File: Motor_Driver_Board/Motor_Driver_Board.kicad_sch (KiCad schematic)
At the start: 33 parts, among them J1 POWER, J2 MOTOR, J3 LCD, SW1 ENCODER, U1 XL1509-5.0

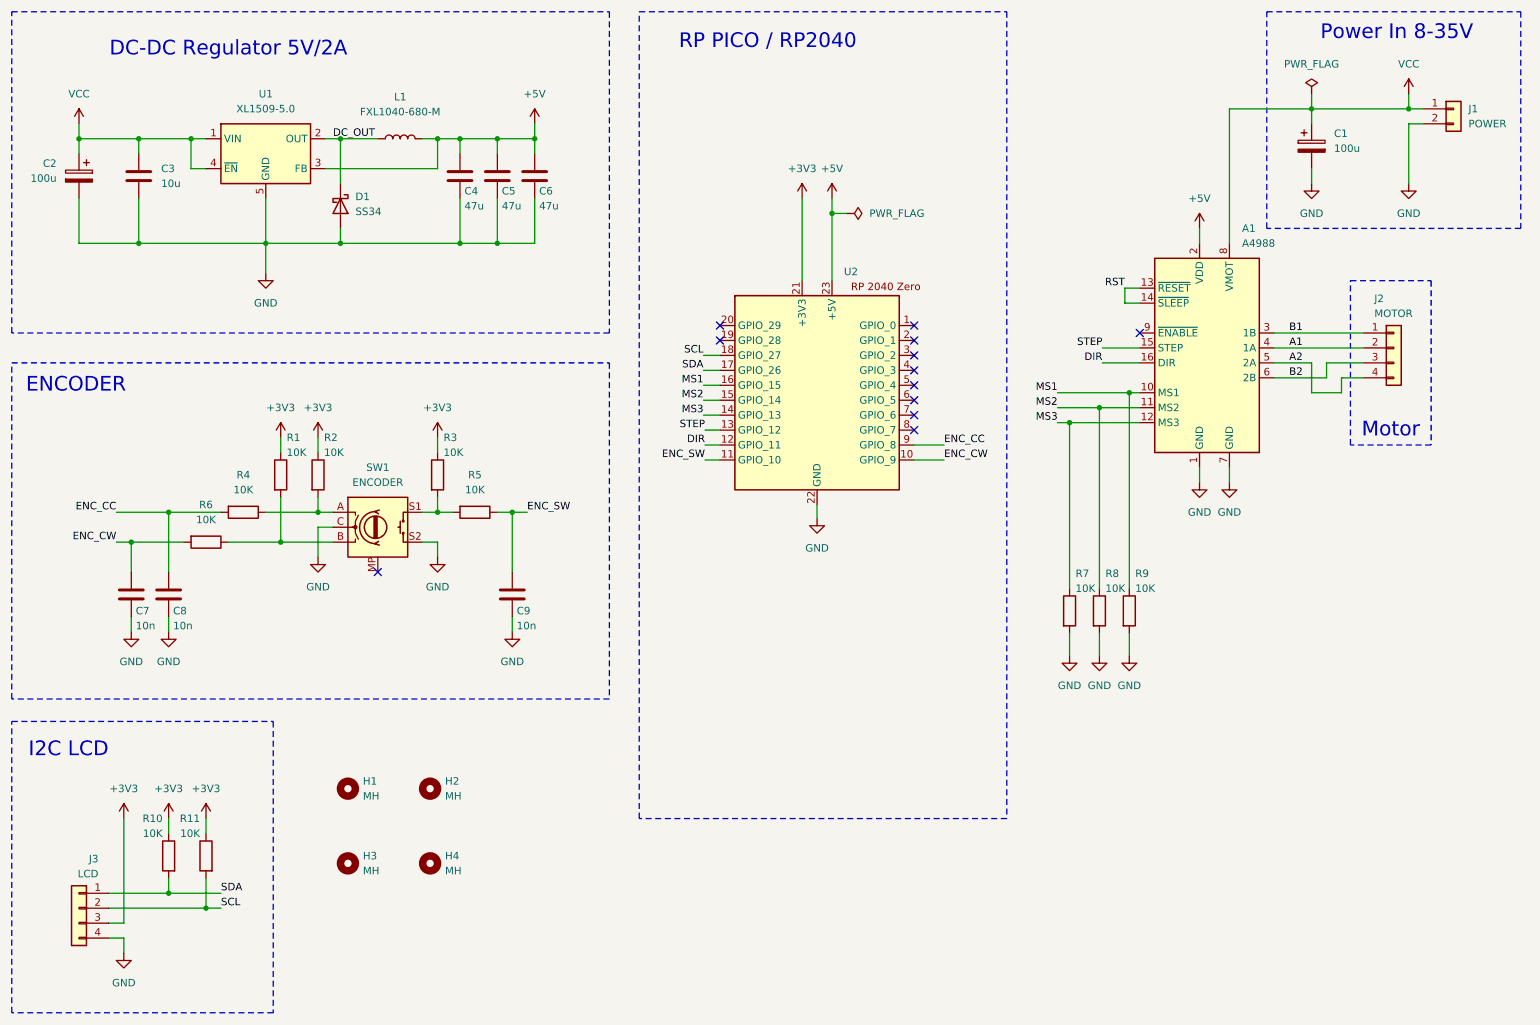
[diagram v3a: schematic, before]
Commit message: Layout revision
Updated the schematic pinout for the RP2040.
Updated the PCB layout.
Rotated the motor driver.
Moved the motor header to the side of the board.
Added via stitching.
Removed vias in pads.
Removed length matching from traces.
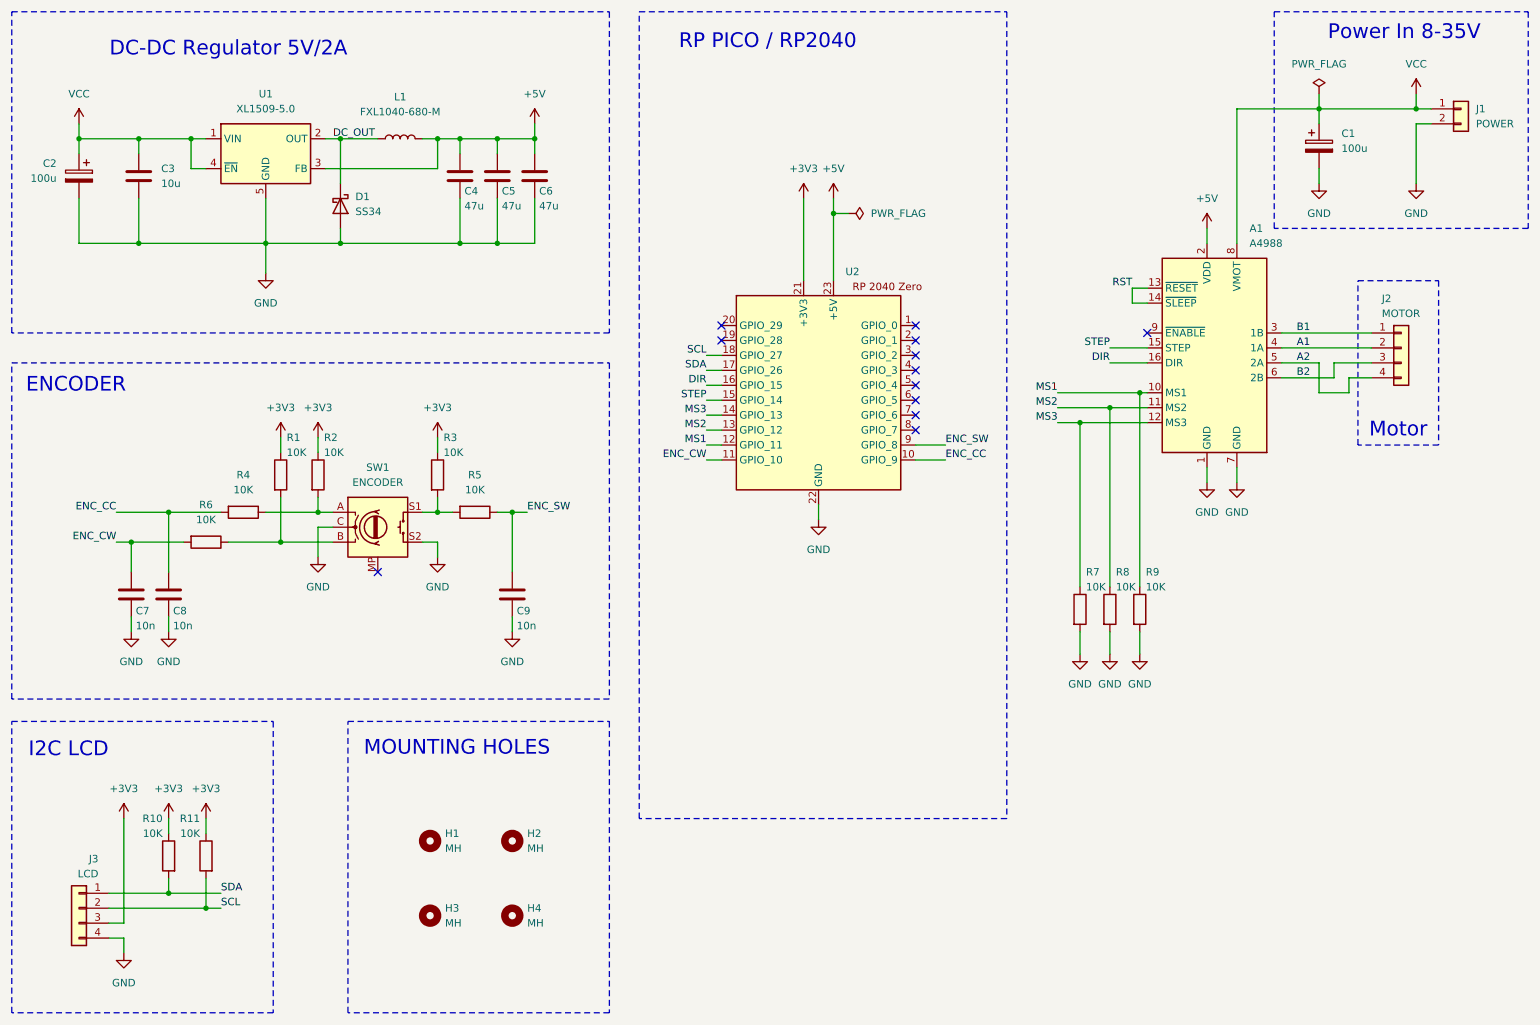
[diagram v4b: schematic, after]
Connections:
- net DIR: now also U2.16 (GPIO_15); no longer U2.12 (GPIO_11)
- net ENC_CC: now also U2.10 (GPIO_9); no longer U2.9 (GPIO_8)
- net ENC_CW: now also U2.11 (GPIO_10); no longer U2.10 (GPIO_9)
- net ENC_SW: now also U2.9 (GPIO_8); no longer U2.11 (GPIO_10)
- net MS1: now also U2.12 (GPIO_11); no longer U2.16 (GPIO_15)
- net MS2: now also U2.13 (GPIO_12); no longer U2.15 (GPIO_14)
- net STEP: now also U2.15 (GPIO_14); no longer U2.13 (GPIO_12)
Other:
- note added: "MOUNTING HOLES"
- moved on the sheet: A1, C1, H1, H2, H3, H4, J1, J2, R7, R8, R9

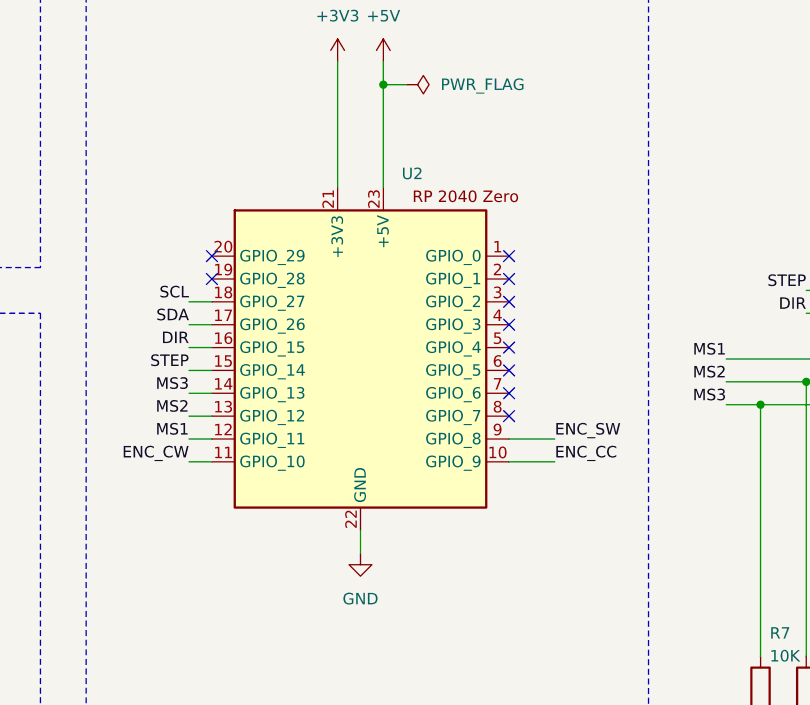
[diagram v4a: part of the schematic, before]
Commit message: PCB layout and models
Updated the PCB layout.
Updated the models for the MCU, motor driver and encoder.
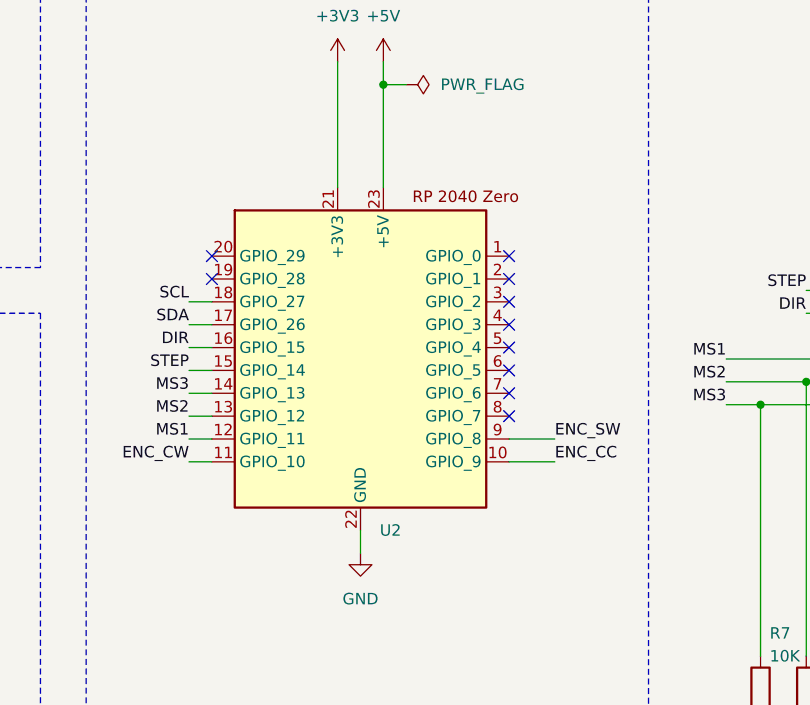
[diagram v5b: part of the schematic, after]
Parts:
- removed U2: (no value), RP2040Zero:MODULE_RP2040-ZERO, symbol RP2040_Zero:RP2040_Zero
- added U2: (no value), Custom_Parts:MODULE_RP2040-ZERO, symbol Custom_Parts:RP2040_Zero
- A1: footprint Module:Pololu_Breakout-16_15.2x20.3mm -> Custom_Parts:MODULE_A4988_STEPPER_MOTOR_DRIVER_CARRIER
- J3: footprint Connector_PinHeader_2.54mm:PinHeader_1x04_P2.54mm_Vertical -> Connector_PinSocket_2.54mm:PinSocket_1x04_P2.54mm_Vertical
- SW1: footprint Rotary_Encoder:RotaryEncoder_Alps_EC11E-Switch_Vertical_H20mm_CircularMountingHoles -> Custom_Parts:RotaryEncoder_Alps_EC11E
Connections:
- net +3V3: now also U2.21 (+3V3)
- net +5V: now also U2.23 (+5V)
- net DIR: now also U2.16 (GPIO_15)
- net ENC_CC: now also U2.10 (GPIO_9)
- net ENC_CW: now also U2.11 (GPIO_10)
- net ENC_SW: now also U2.9 (GPIO_8)
- net GND: now also U2.22 (GND)
- net MS1: now also U2.12 (GPIO_11)
- net MS2: now also U2.13 (GPIO_12)
- net MS3: now also U2.14 (GPIO_13)
- net SCL: now also U2.18 (GPIO_27)
- net SDA: now also U2.17 (GPIO_26)
- net STEP: now also U2.15 (GPIO_14)
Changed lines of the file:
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@@
 			)
 		)
-		(property "Footprint" "Rotary_Encoder:RotaryEncoder_Alps_EC11E-Switch_Vertical_H20mm_CircularMountingHoles"
+		(property "Footprint" "Custom_Parts:RotaryEncoder_Alps_EC11E"
 			(at 78.74 106.426 0)
 			(hide yes)
@@
 			)
 		)
-		(property "Footprint" "Module:Pololu_Breakout-16_15.2x20.3mm"
+		(property "Footprint" "Custom_Parts:MODULE_A4988_STEPPER_MOTOR_DRIVER_CARRIER"
 			(at 230.505 99.06 0)
 			(hide yes)
@@
 			)
 		)
-		(property "Footprint" "Connector_PinHeader_2.54mm:PinHeader_1x04_P2.54mm_Vertical"
+		(property "Footprint" "Connector_PinSocket_2.54mm:PinSocket_1x04_P2.54mm_Vertical"
 			(at 31.75 175.26 0)
 			(hide yes)
@@
 	)
 	(symbol
+		(lib_id "Custom_Parts:RP2040_Zero")
+		(at 157.48 83.82 0)
+		(unit 1)
+		(body_style 1)
+		(exclude_from_sim no)
+		(in_bom yes)
+		(on_board yes)
+		(in_pos_files yes)
+		(dnp no)
+		(fields_autoplaced yes)
+		(property "Reference" "U2"
+			(at 159.6233 106.68 0)
+			(show_name no)
+			(do_not_autoplace no)
+			(effects
+				(font
+					(size 1.27 1.27)
+				)
+				(justify left)
+			)
+		)
+		(property "Value" ""
+			(at 157.48 83.82 0)
+			(show_name no)
+			(do_not_autoplace no)
+			(effects
+				(font
+					(size 1.27 1.27)
+				)
+			)
+		)
+		(property "Footprint" "Custom_Parts:MODULE_RP2040-ZERO"
+			(at 157.48 83.82 0)
+			(hide yes)
+			(show_name no)
+			(do_not_autoplace no)
+			(effects
+				(font
+					(size 1.27 1.27)
+				)
+			)
+		)
+		(property "Datasheet" ""
+			(at 157.48 83.82 0)
+			(hide yes)
+			(show_name no)
+			(do_not_autoplace no)
+			(effects
+				(font
+					(size 1.27 1.27)
+				)
+			)
+		)
+		(property "Description" ""
+			(at 157.48 83.82 0)
+			(hide yes)
+			(show_name no)
+			(do_not_autoplace no)
+			(effects
+				(font
+					(size 1.27 1.27)
+				)
+			)
+		)
+		(pin "18"
+		)
+		(pin "20"
+		)
+		(pin "8"
+		)
+		(pin "17"
+		)
+		(pin "4"
+		)
+		(pin "1"
+		)
+		(pin "11"
+		)
+		(pin "6"
+		)
+		(pin "7"
+		)
+		(pin "3"
+		)
+		(pin "13"
+		)
+		(pin "12"
+		)
+		(pin "2"
+		)
+		(pin "5"
+		)
+		(pin "14"
+		)
+		(pin "10"
+		)
+		(pin "9"
+		)
+		(pin "15"
+		)
+		(pin "16"
+		)
+		(pin "19"
+		)
+		(pin "22"
+		)
+		(pin "23"
+		)
+		(pin "21"
+		)
+		(instances
+			(project "Motor_Driver_Board"
+				(path "/c70df163-fa29-4f73-9cea-7339cbbc421d"
+					(reference "U2")
+					(unit 1)
+				)
+			)
+		)
+	)
+	(symbol
 		(lib_id "Device:R")
 		(at 207.01 124.46 0)
@@
 					(unit 1)
 				)
-			)
-		)
-	)
-	(symbol
-		(lib_id "RP2040_Zero:RP2040_Zero")
-		(at 157.48 83.82 0)
-		(unit 1)
-		(body_style 1)
-		(exclude_from_sim no)
-		(in_bom yes)
-		(on_board yes)
-		(in_pos_files yes)
-		(dnp no)
-		(property "Reference" "U2"
-			(at 162.052 67.056 0)
-			(show_name no)
-			(do_not_autoplace no)
-			(effects
-				(font
-					(size 1.27 1.27)
-				)
-				(justify left)
-			)
-		)
-		(property "Value" ""
-			(at 157.48 83.82 0)
-			(show_name no)
-			(do_not_autoplace no)
-			(effects
-				(font
-					(size 1.27 1.27)
-				)
-			)
-		)
-		(property "Footprint" "RP2040Zero:MODULE_RP2040-ZERO"
-			(at 157.48 83.82 0)
-			(hide yes)
-			(show_name no)
-			(do_not_autoplace no)
-			(effects
-				(font
-					(size 1.27 1.27)
-				)
-			)
-		)
-		(property "Datasheet" ""
-			(at 157.48 83.82 0)
-			(hide yes)
-			(show_name no)
-			(do_not_autoplace no)
-			(effects
-				(font
-					(size 1.27 1.27)
-				)
-			)
-		)
-		(property "Description" ""
-			(at 157.48 83.82 0)
-			(hide yes)
-			(show_name no)
-			(do_not_autoplace no)
-			(effects
-				(font
-					(size 1.27 1.27)
-				)
-			)
-		)
-		(pin "10"
-		)
-		(pin "5"
-		)
-		(pin "4"
-		)
-		(pin "17"
-		)
-		(pin "2"
-		)
-		(pin "6"
-		)
-		(pin "8"
-		)
-		(pin "18"
-		)
-		(pin "12"
-		)
-		(pin "7"
-		)
-		(pin "1"
-		)
-		(pin "3"
-		)
-		(pin "9"
-		)
-		(pin "13"
-		)
-		(pin "14"
-		)
-		(pin "19"
-		)
-		(pin "20"
-		)
-		(pin "16"
-		)
-		(pin "15"
-		)
-		(pin "11"
-		)
-		(pin "22"
-		)
-		(pin "21"
-		)
-		(pin "23"
-		)
-		(instances
-			(project "Motor_Driver_Board"
-				(path "/c70df163-fa29-4f73-9cea-7339cbbc421d"
-					(reference "U2")
-					(unit 1)
-				)

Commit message: Build outputs
Added the intial build files.
Added the part numbers for all components.
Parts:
- A1: JLCPCB Part (none) -> -; Manufacturer Part (none) -> -; now left out of the parts list
- C1, C2: JLCPCB Part (none) -> C46550435; Manufacturer Part (none) -> PA35V100M6x8; now left out of the parts list
- C3: JLCPCB Part (none) -> C13585; Manufacturer Part (none) -> CL31A106KBHNNNE
- C4, C5, C6: JLCPCB Part (none) -> C96123; Manufacturer Part (none) -> CL31A476MPHNNNE
- C7, C8, C9: JLCPCB Part (none) -> C57112; Manufacturer Part (none) -> 0603B103K500NT
- D1: JLCPCB Part (none) -> C8678; Manufacturer Part (none) -> SS34
- H1, H2, H3, H4: JLCPCB Part (none) -> -; Manufacturer Part (none) -> -
- J1: JLCPCB Part (none) -> C492401; Manufacturer Part (none) -> PZ254V-11-02P; now left out of the parts list
- J2, J3: JLCPCB Part (none) -> C2691448; Manufacturer Part (none) -> PZ254V-11-04P; now left out of the parts list
- L1: JLCPCB Part (none) -> C475920; Manufacturer Part (none) -> FXL1040-680-M
- R1, R10, R11, R2, R3, R4, R5, R6, R7, R8, R9: JLCPCB Part (none) -> C25804; Manufacturer Part (none) -> 0603WAF1002T5E
- SW1: JLCPCB Part (none) -> C202365; Manufacturer Part (none) -> EC11E18244AU; now left out of the parts list
- U1: JLCPCB Part (none) -> C61063; Manufacturer Part (none) -> XL1509-5.0E1
- U2: JLCPCB Part (none) -> C5350143; Manufacturer Part (none) -> RP2040-Zero; now left out of the parts list

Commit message: Footprints
Updated the footprint for the bulk capacitors.
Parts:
- C1, C2: footprint Capacitor_THT:CP_Radial_D6.3mm_P2.50mm -> Capacitor_THT:CP_Radial_D8.0mm_P3.50mm
- U2: Manufacturer Part RP2040-Zero -> RP2040-Zero
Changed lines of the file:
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@@
 			)
 		)
-		(property "Footprint" "Capacitor_THT:CP_Radial_D6.3mm_P2.50mm"
+		(property "Footprint" "Capacitor_THT:CP_Radial_D8.0mm_P3.50mm"
 			(at 30.7848 54.61 0)
 			(hide yes)
@@
 			)
 		)
-		(property "Manufacturer Part" "     RP2040-Zero"
+		(property "Manufacturer Part" "RP2040-Zero"
 			(at 157.48 83.82 0)
 			(hide yes)
@@
 			)
 		)
-		(property "Footprint" "Capacitor_THT:CP_Radial_D6.3mm_P2.50mm"
+		(property "Footprint" "Capacitor_THT:CP_Radial_D8.0mm_P3.50mm"
 			(at 243.5352 49.53 0)
 			(hide yes)

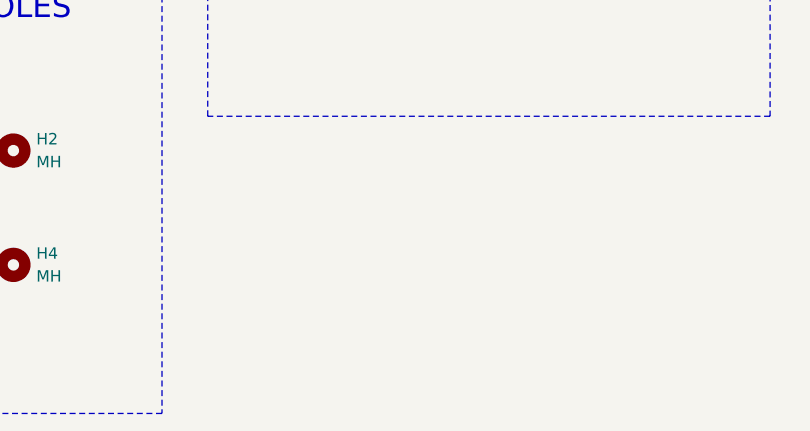
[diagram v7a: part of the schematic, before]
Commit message: Tooling and silkscreen
Updated the silkscreen.
Added tooling holes for the assembly service.
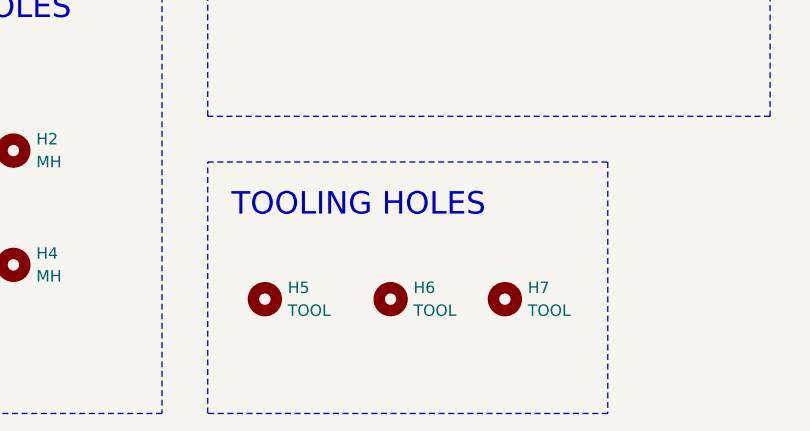
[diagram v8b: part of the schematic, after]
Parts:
- added H5, H6, H7: TOOL, MountingHole:ToolingHole_1.152mm, symbol Mechanical:MountingHole
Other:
- note added: "TOOLING HOLES"
